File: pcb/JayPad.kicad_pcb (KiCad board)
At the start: 2 copper layers, 113 x 70.8 mm, 51 parts, among them M1 MOUDLE-SEEEDUINO-XIAO, SW1 PEC11-4215F-S24

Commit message: Fixed incorrect switch references
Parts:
- renumbered S4 to S1, S11 to S10, S10 to S11, S9 to S12, S3 to S2, S2 to S3, S1 to S4, S8 to S5, S7 to S6, S6 to S7, S5 to S8, S12 to S9
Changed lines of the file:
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@@
 		(descr "Cherry MX switch footprint. Size: 1.00u, Mount type: Plate, Using Kailh Socket: yes, Stabilizer: n/a, Lighting: LTST-A683CEGBW for hand-soldering")
 		(tags "CherryMX 1.00u KailhSocket LTST-A683CEGBW-HS")
-		(property "Reference" "S5"
+		(property "Reference" "S8"
 			(at 58.73 -8.6625 0)
 			(layer "B.SilkS")
@@
 		(descr "Cherry MX switch footprint. Size: 1.00u, Mount type: Plate, Using Kailh Socket: yes, Stabilizer: n/a, Lighting: LTST-A683CEGBW for hand-soldering")
 		(tags "CherryMX 1.00u KailhSocket LTST-A683CEGBW-HS")
-		(property "Reference" "S2"
+		(property "Reference" "S3"
 			(at 19.51 -8.6625 0)
 			(layer "B.SilkS")
@@
 		(descr "Cherry MX switch footprint. Size: 1.00u, Mount type: Plate, Using Kailh Socket: yes, Stabilizer: n/a, Lighting: LTST-A683CEGBW for hand-soldering")
 		(tags "CherryMX 1.00u KailhSocket LTST-A683CEGBW-HS")
-		(property "Reference" "S9"
+		(property "Reference" "S12"
 			(at 58.77 -8.6625 0)
 			(layer "B.SilkS")
@@
 		(descr "Cherry MX switch footprint. Size: 1.00u, Mount type: Plate, Using Kailh Socket: yes, Stabilizer: n/a, Lighting: LTST-A683CEGBW for hand-soldering")
 		(tags "CherryMX 1.00u KailhSocket LTST-A683CEGBW-HS")
-		(property "Reference" "S12"
+		(property "Reference" "S9"
 			(at -58.99 -8.6625 0)
 			(layer "B.SilkS")
@@
 		(descr "Cherry MX switch footprint. Size: 1.00u, Mount type: Plate, Using Kailh Socket: yes, Stabilizer: n/a, Lighting: LTST-A683CEGBW for hand-soldering")
 		(tags "CherryMX 1.00u KailhSocket LTST-A683CEGBW-HS")
-		(property "Reference" "S1"
+		(property "Reference" "S4"
 			(at 58.73 -8.6625 0)
 			(layer "B.SilkS")
@@
 		(descr "Cherry MX switch footprint. Size: 1.00u, Mount type: Plate, Using Kailh Socket: yes, Stabilizer: n/a, Lighting: LTST-A683CEGBW for hand-soldering")
 		(tags "CherryMX 1.00u KailhSocket LTST-A683CEGBW-HS")
-		(property "Reference" "S7"
+		(property "Reference" "S6"
 			(at -19.77 -8.6625 0)
 			(layer "B.SilkS")
@@
 		(descr "Cherry MX switch footprint. Size: 1.00u, Mount type: Plate, Using Kailh Socket: yes, Stabilizer: n/a, Lighting: LTST-A683CEGBW for hand-soldering")
 		(tags "CherryMX 1.00u KailhSocket LTST-A683CEGBW-HS")
-		(property "Reference" "S8"
+		(property "Reference" "S5"
 			(at -58.97 -8.6625 0)
 			(layer "B.SilkS")
@@
 		(descr "Cherry MX switch footprint. Size: 1.00u, Mount type: Plate, Using Kailh Socket: yes, Stabilizer: n/a, Lighting: LTST-A683CEGBW for hand-soldering")
 		(tags "CherryMX 1.00u KailhSocket LTST-A683CEGBW-HS")
-		(property "Reference" "S3"
+		(property "Reference" "S2"
 			(at -19.77 -8.6625 0)
 			(layer "B.SilkS")
@@
 		(descr "Cherry MX switch footprint. Size: 1.00u, Mount type: Plate, Using Kailh Socket: yes, Stabilizer: n/a, Lighting: LTST-A683CEGBW for hand-soldering")
 		(tags "CherryMX 1.00u KailhSocket LTST-A683CEGBW-HS")
-		(property "Reference" "S6"
+		(property "Reference" "S7"
 			(at 19.49 -8.6625 0)
 			(layer "B.SilkS")
@@
 		(descr "Cherry MX switch footprint. Size: 1.00u, Mount type: Plate, Using Kailh Socket: yes, Stabilizer: n/a, Lighting: LTST-A683CEGBW for hand-soldering")
 		(tags "CherryMX 1.00u KailhSocket LTST-A683CEGBW-HS")
-		(property "Reference" "S10"
+		(property "Reference" "S11"
 			(at 19.54 -8.6625 0)
 			(layer "B.SilkS")
@@
 		(descr "Cherry MX switch footprint. Size: 1.00u, Mount type: Plate, Using Kailh Socket: yes, Stabilizer: n/a, Lighting: LTST-A683CEGBW for hand-soldering")
 		(tags "CherryMX 1.00u KailhSocket LTST-A683CEGBW-HS")
-		(property "Reference" "S11"
+		(property "Reference" "S10"
 			(at -19.71 -8.6625 0)
 			(layer "B.SilkS")
@@
 		(descr "Cherry MX switch footprint. Size: 1.00u, Mount type: Plate, Using Kailh Socket: yes, Stabilizer: n/a, Lighting: LTST-A683CEGBW for hand-soldering")
 		(tags "CherryMX 1.00u KailhSocket LTST-A683CEGBW-HS")
-		(property "Reference" "S4"
+		(property "Reference" "S1"
 			(at -58.99 -8.6625 0)
 			(layer "B.SilkS")

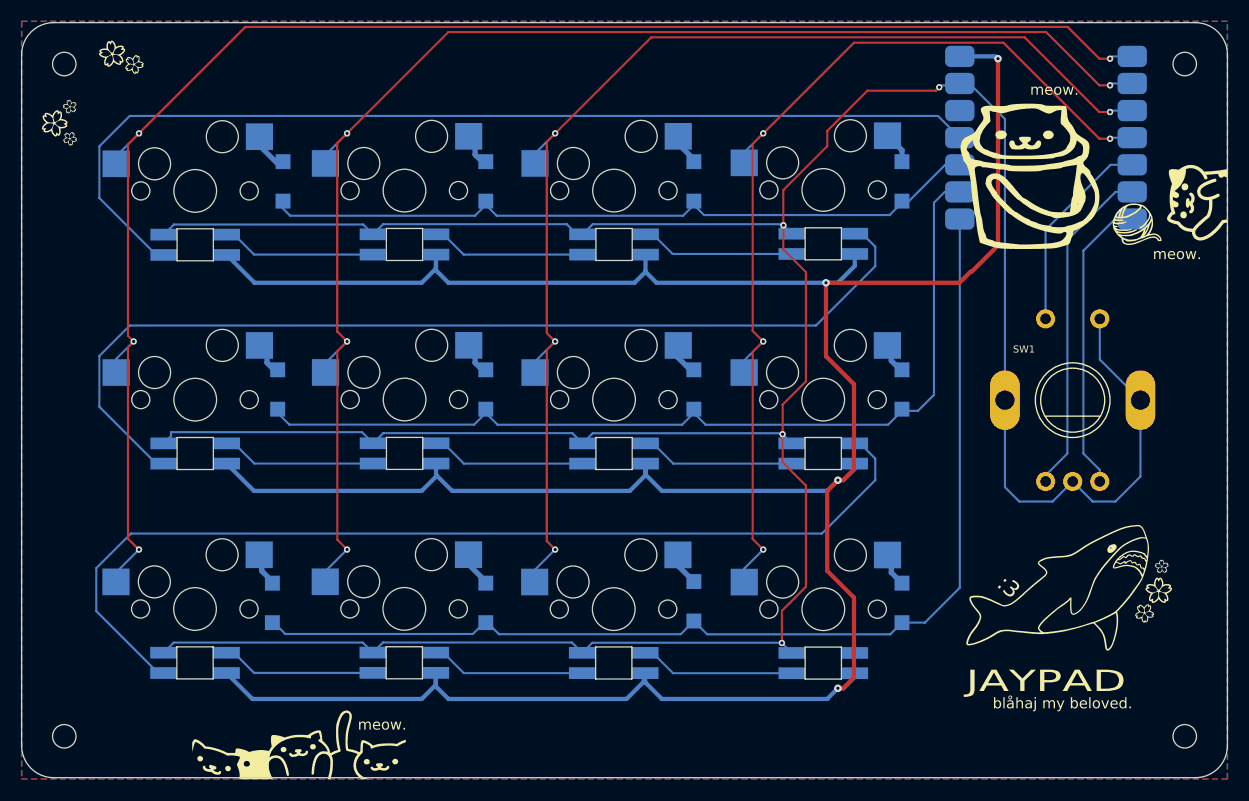
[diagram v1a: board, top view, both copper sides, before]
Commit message: Copper zone set to GND, optimised COL & GND traces
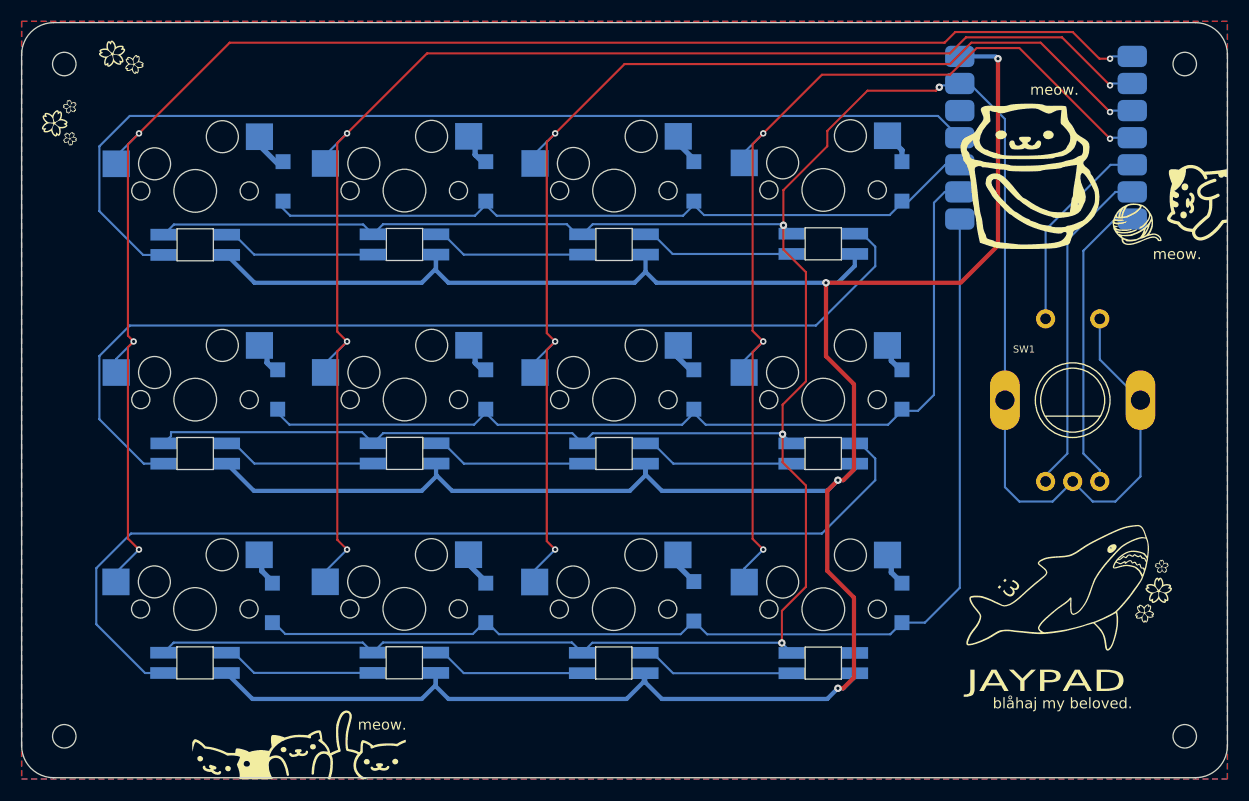
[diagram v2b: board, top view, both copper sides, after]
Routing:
- net Net-(S8-DOUT): track 93.7 -> 94.4 mm
- net RGB: track 95.7 -> 96.5 mm
- net Net-(S4-DOUT): track 93.5 -> 94.1 mm
- added copper zone on B.Cu, net GND
- added copper zone on F.Cu, net GND
- removed copper zone on B.Cu, net (none)
- removed copper zone on F.Cu, net (none)

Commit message: Fixed GND traces not following DRC
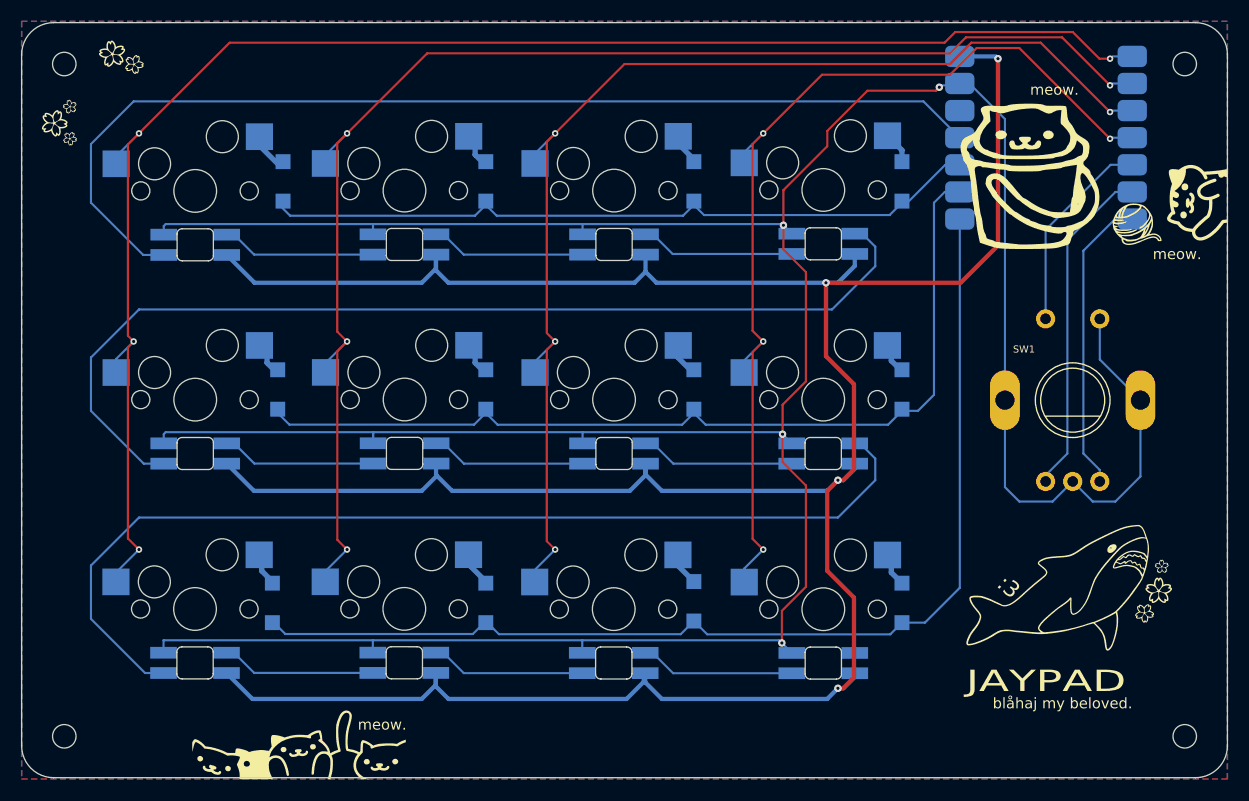
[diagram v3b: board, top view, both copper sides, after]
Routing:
- net GND: track 323.4 -> 327.7 mm
- net RGB: track 96.5 -> 98.8 mm
- net Net-(S4-DOUT): track 94.1 -> 95.2 mm
- net Net-(S8-DOUT): track 94.4 -> 95.3 mm
